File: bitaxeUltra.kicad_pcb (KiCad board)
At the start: 4 copper layers, 85 x 56 mm, 87 parts, among them J1 Barrel_Jack_Switch, J2 Conn_02x20_Odd_Even, J3 Conn_01x05, M1 Fan_4pin, Q1 CSD16321Q5, Q2 CSD16321Q5, Q3 BSS138, Q4 BSS138, Q5 BSS138, Q9 BSS138, U1 TPS40304DRC, U14 BM1366_mode1, U5 MCP1824T-1802E, U6 MCP1824T-0802E, U7 25MHz

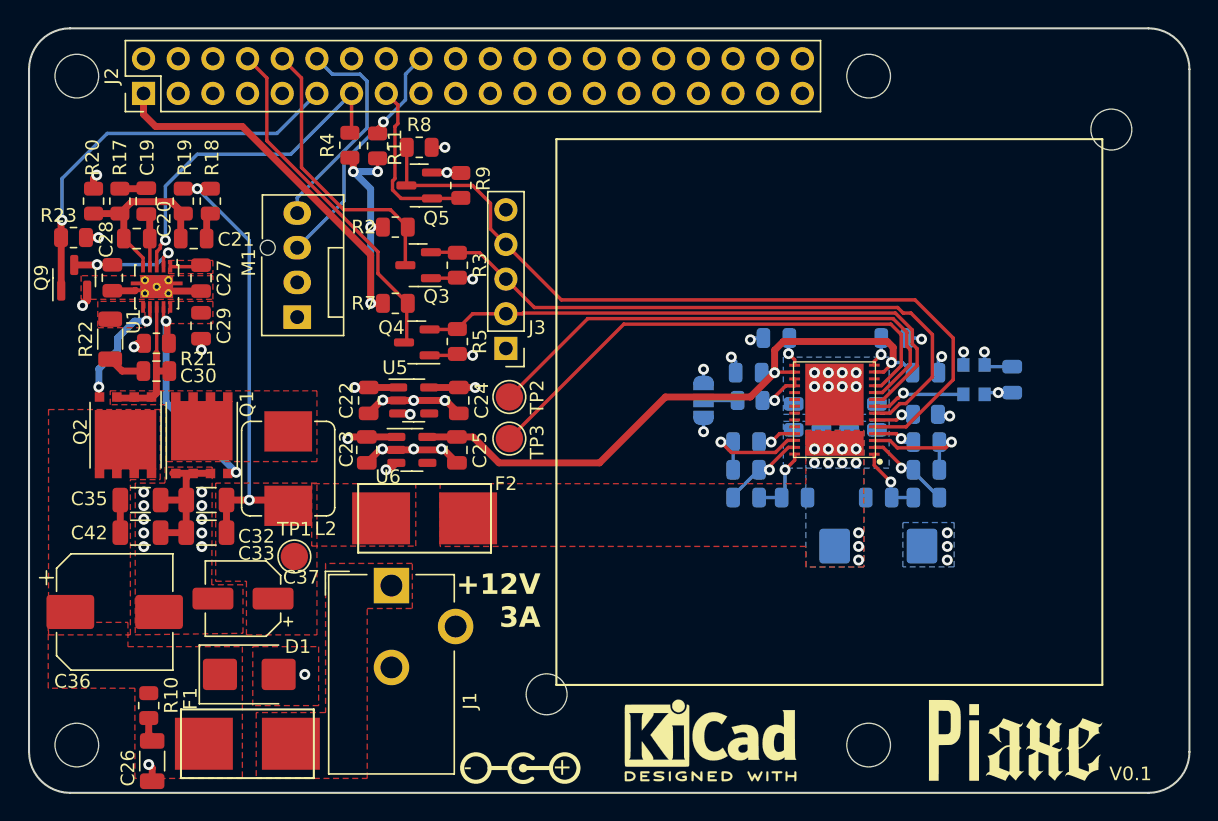
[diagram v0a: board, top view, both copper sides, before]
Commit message: added back the two 1uF
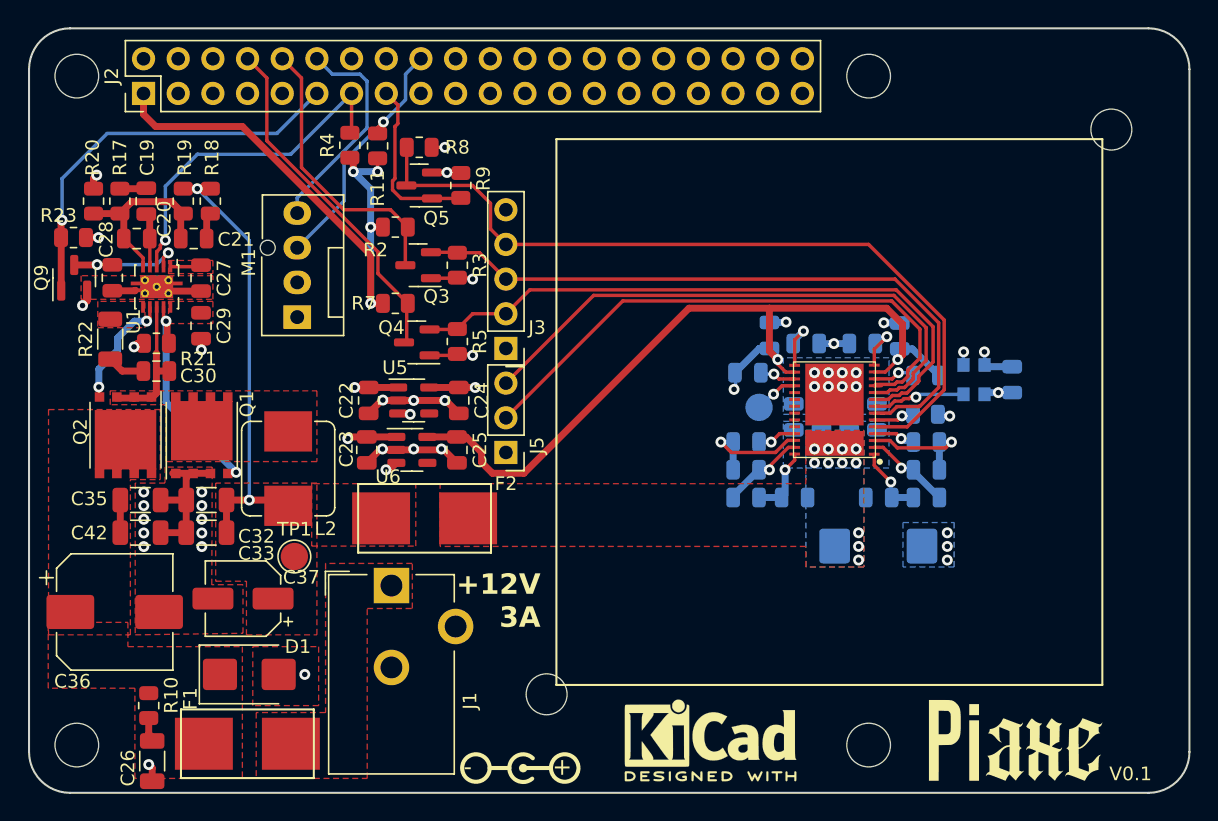
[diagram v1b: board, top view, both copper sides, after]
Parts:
- removed JP1: mode, Jumper:SolderJumper-3_P1.3mm_Open_RoundedPad1.0x1.5mm
- removed R1: 10k, Resistor_SMD:R_0805_2012Metric
- removed TP3: TEMP_n, TestPoint:TestPoint_Pad_D2.0mm
- added C31: 1µ, Capacitor_SMD:C_0805_2012Metric, B.Cu at (239.0, 81.2)
- added C34: 1µ, Capacitor_SMD:C_0805_2012Metric, B.Cu at (226.0, 81.0)
- added J5: temp, Connector_PinHeader_2.54mm:PinHeader_1x03_P2.54mm_Vertical, F.Cu at (208.3, 86.9)
- C32, C33: value 47µ -> 47µ/10V
- C35, C42: value 10µ -> 10µ/25V
- TP2: value TEMP_P -> TestPoint; moved to B.Cu
- moved TP2 18.3 mm to (226.8, 83.6), turned to 180 degrees
- moved C5 9.15 mm to (227.6, 78.3), turned to 90 degrees
- moved C16 8.60 mm to (234.4, 78.9)
- moved C4 3.28 mm to (237.1, 78.3), turned to 90 degrees
- moved C14 2.22 mm to (230.3, 78.9), turned to 0 degrees
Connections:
- C16 pad 1: +0V8 -> +1V8
- C5 pad 1: +1V8 -> +0V8
- TP2 pad 1: /BM1366/TEMP_P -> Net-(U14-MODE_0)
- U14 pad 12: unconnected-(U14-MODEO-Pad12) -> Net-(U14-MODEO)
- U14 pad 17: Net-(U14-MODE_0) -> Net-(U14-MODE_1)
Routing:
- net +0V8: track 46.8 -> 62.6 mm, vias 2 -> 3
- net /BM1366/TEMP_N: track 37.4 -> 41.8 mm
- net /BM1366/CI: track 43.3 -> 47.4 mm
- net /BM1366/TEMP_P: track 37.9 -> 41.8 mm
- net Net-(U14-MODEO): track 0.00 -> 3.11 mm, vias 0 -> 1
- net Net-(U14-MODE_1): track 0.00 -> 2.66 mm, vias 0 -> 1
- net Net-(JP1-C): track 2.49 -> 0.00 mm
- net +1V8: track 20.1 -> 22.2 mm, vias 9 -> 8
- net /BM1366/RO: track 47.7 -> 49.6 mm
- net GND: track 97.5 -> 96.4 mm, vias 42 -> 40

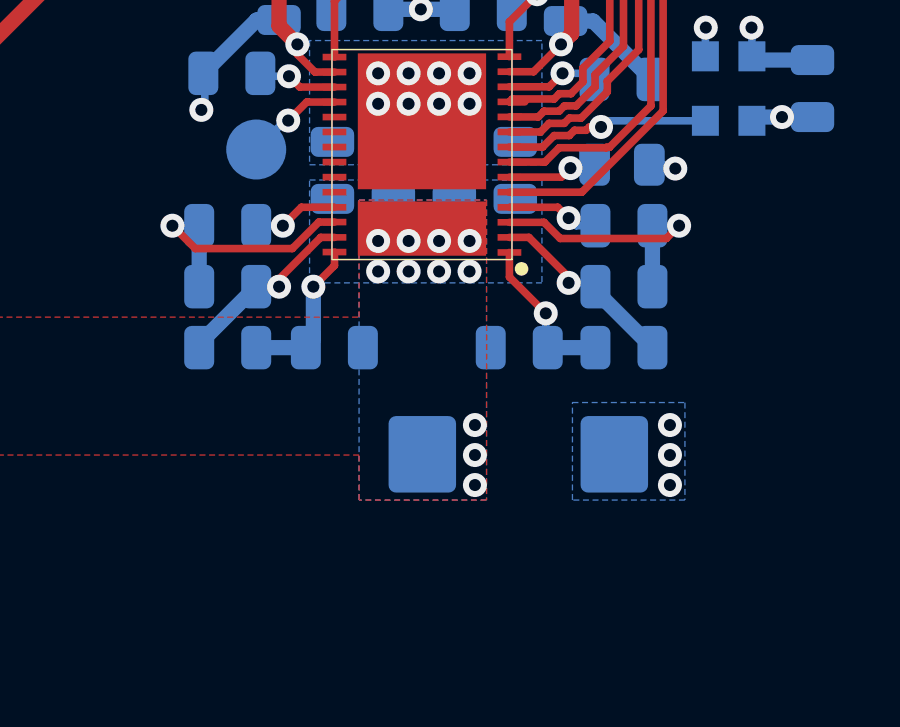
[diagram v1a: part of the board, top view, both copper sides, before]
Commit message: removed tantal and replaced with ceramic caps
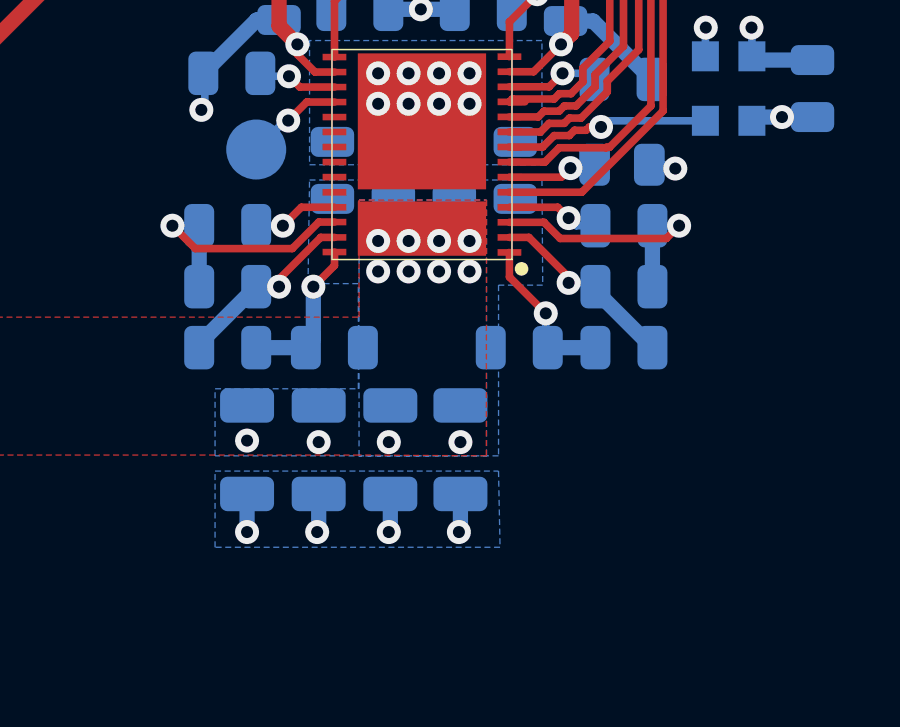
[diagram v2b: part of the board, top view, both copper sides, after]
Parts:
- removed C13: 330µ, Capacitor_Tantalum_SMD:CP_EIA-7343-31_Kemet-D_Pad2.25x2.55mm_HandSolder
- added C38: 10µ/25V, Capacitor_SMD:C_1206_3216Metric, B.Cu at (233.6, 93.6)
- added C39: 10µ/25V, Capacitor_SMD:C_1206_3216Metric, B.Cu at (231.3, 93.6)
- added C40: 47µ/10V, Capacitor_SMD:C_1206_3216Metric, B.Cu at (226.5, 93.6)
- added C41: 47µ/10V, Capacitor_SMD:C_1206_3216Metric, B.Cu at (228.9, 93.6)
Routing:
- net GND: track 96.4 -> 101.6 mm, vias 40 -> 41
- net +1V5: vias 11 -> 12

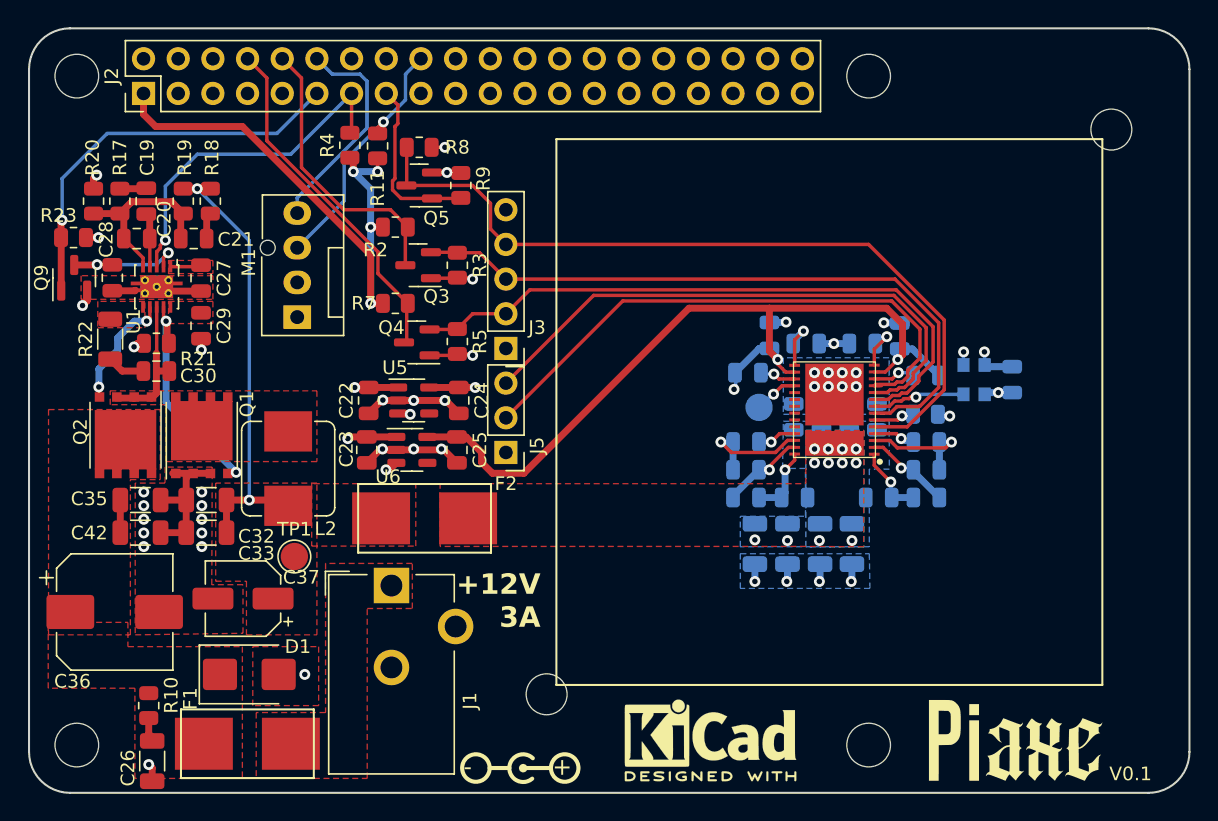
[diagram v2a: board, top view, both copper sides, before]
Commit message: revised heat-sinking. Supports heatsinks with 40x40 size with holes 35x35, 32x32 and 33x33
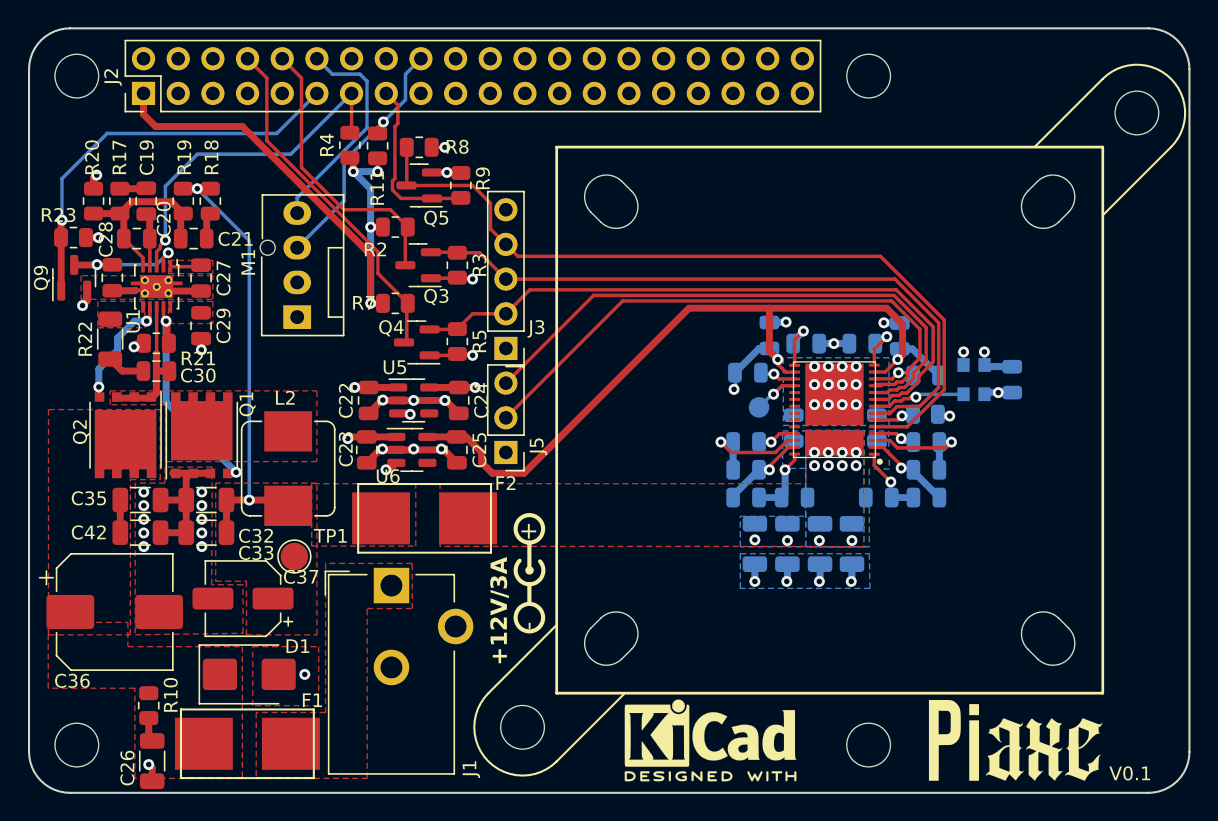
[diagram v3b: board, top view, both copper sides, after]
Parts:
- removed H5, H6: MountingHole, MountingHole:MountingHole_3.5mm
- added REF**: MountingHole_3.2mm_M3, MountingHole:MountingHole_3.2mm_M3, F.Cu at (254.5, 62.0)
- added REF**: MountingHole_3.2mm_M3, MountingHole:MountingHole_3.2mm_M3, F.Cu at (209.5, 107.0)
- TP2: footprint TestPoint:TestPoint_Pad_D2.0mm -> TestPoint:TestPoint_Pad_D1.5mm
- moved U3 14.5 mm to (210.0, 95.5), turned to 90 degrees
- moved C10 0.83 mm to (235.5, 85.1)
- moved C11 0.83 mm to (229.4, 85.1)
- moved C7 0.83 mm to (231.4, 85.1)
- moved C9 0.83 mm to (233.4, 85.1)
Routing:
- net GND: vias 41 -> 45
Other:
- outline, holes or cut-outs redrawn
- board text added: "+12V/3A"
- board text removed: "+12V 3A"

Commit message: added gerbers and bom
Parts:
- added C13: 100n, Capacitor_SMD:C_0805_2012Metric, B.Cu at (225.6, 78.3)
- added C43: 100n, Capacitor_SMD:C_0805_2012Metric, B.Cu at (239.1, 78.3)
- added C44: 100n, Capacitor_SMD:C_0805_2012Metric, B.Cu at (234.4, 76.9)
- added C45: 100n, Capacitor_SMD:C_0805_2012Metric, B.Cu at (230.3, 76.9)
- added JP1: SolderJumper_3_Open, Jumper:SolderJumper-3_P1.3mm_Open_RoundedPad1.0x1.5mm, F.Cu at (192.9, 80.5)
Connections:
- C27 pad 1: Net-(U1-VDD) -> +12V
- M1 pad 2: +5V -> Net-(JP1-C)
- U1 pad 1: Net-(U1-VDD) -> +12V
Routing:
- net +12V: track 2.39 -> 49.0 mm, vias 0 -> 4
- net GND: track 101.6 -> 109.4 mm
- net Net-(JP1-C): track 0.00 -> 7.57 mm
- net +5V: track 57.8 -> 63.3 mm
- net +1V8: track 22.2 -> 26.4 mm
- net +0V8: track 62.6 -> 66.6 mm
- net Net-(U1-VDD): track 2.29 -> 0.00 mm
- removed copper zone on F.Cu, net Net-(U1-VDD)

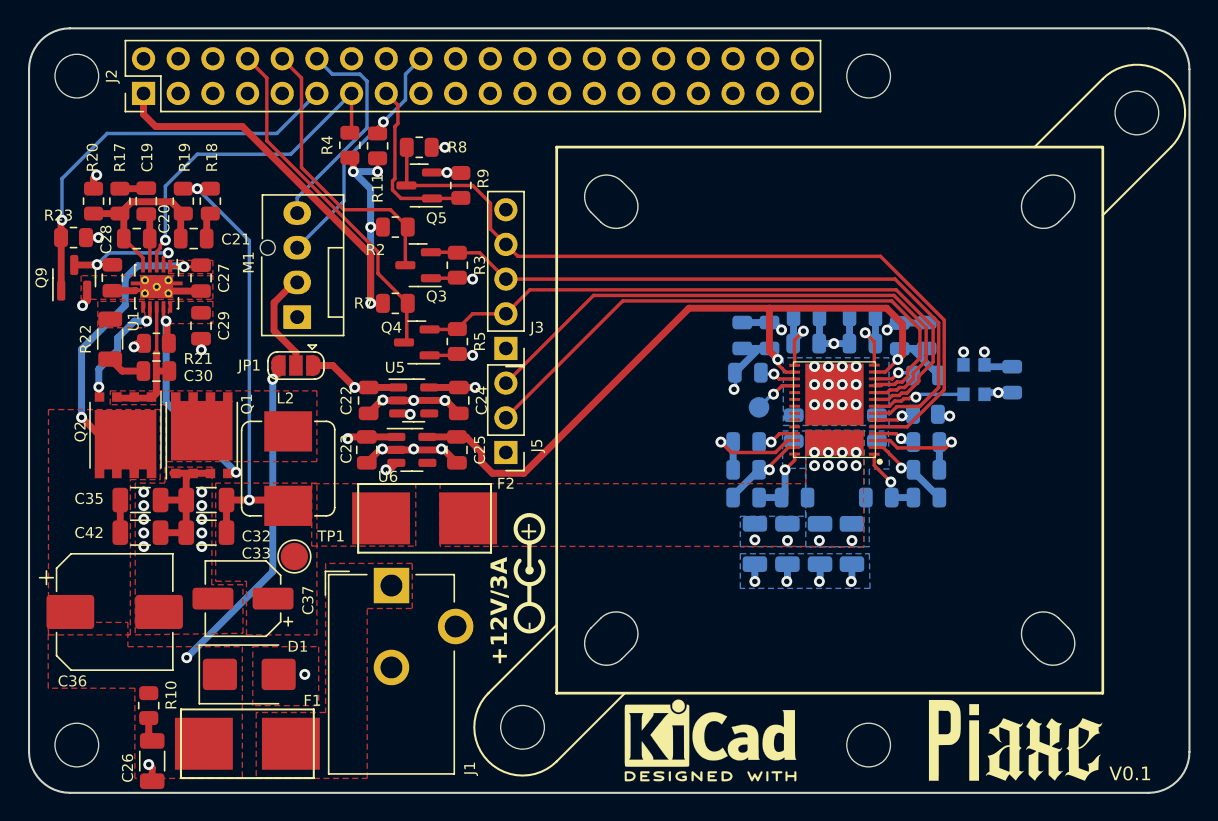
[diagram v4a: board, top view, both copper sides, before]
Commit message: fixed zone-edgecut clearance, added 2nd gnd layer and stitched them together for copper balance
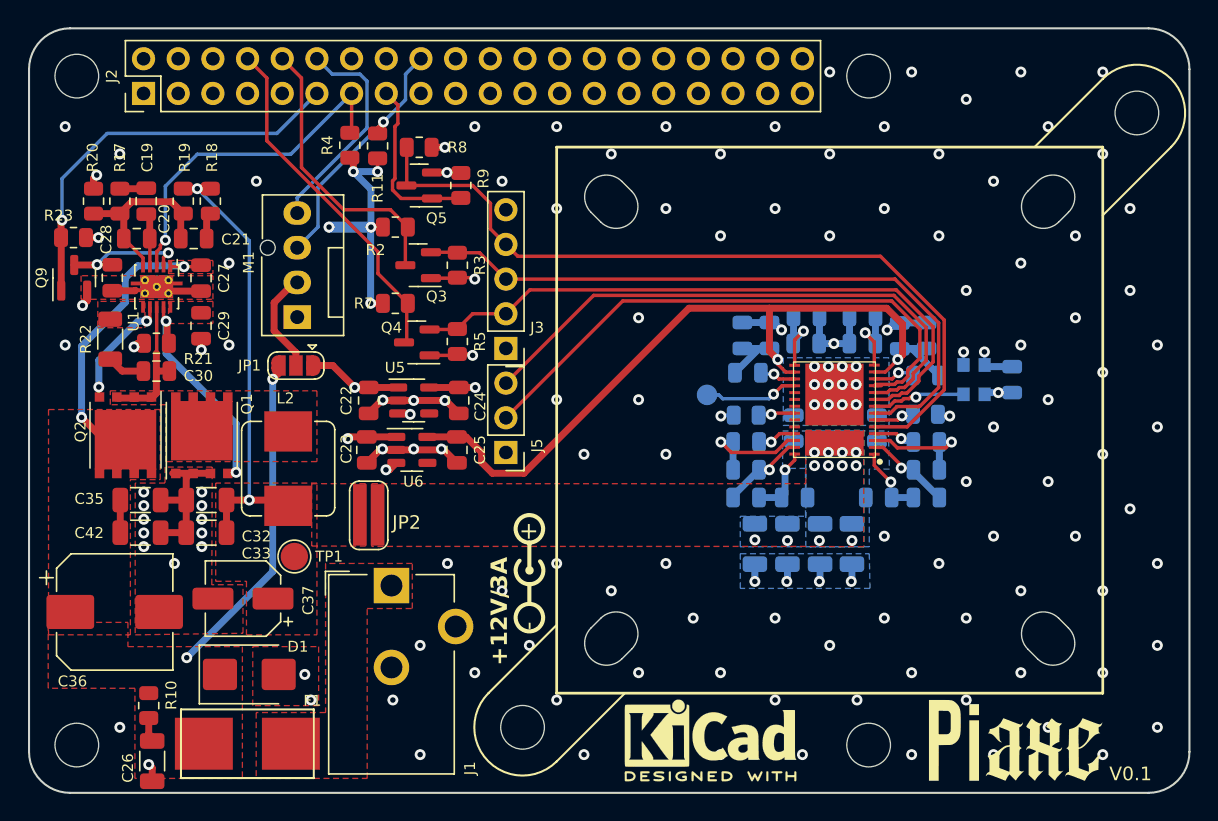
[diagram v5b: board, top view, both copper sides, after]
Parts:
- removed F2: 20A, myfootprints:fuseholder_littlefuse_blok
- added JP2: SolderJumper_2_Open, myfootprints:SolderJumper1.0x4.5, F.Cu at (198.4, 91.7)
- added R1: 10k, Resistor_SMD:R_0805_2012Metric, B.Cu at (225.9, 84.1)
- moved TP2 3.92 mm to (223.0, 82.7)
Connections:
- U14 pad 22: unconnected-(U14-RI-Pad22) -> Net-(U14-RI)
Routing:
- net +1V8: track 26.4 -> 97.5 mm, vias 8 -> 9
- net Net-(U14-MODE_0): track 3.26 -> 7.03 mm
- net +3V3: track 41.7 -> 38.4 mm, vias 4 -> 5
- net Net-(U14-RI): track 0.00 -> 2.70 mm, vias 0 -> 1
- net +0V8: track 66.6 -> 65.3 mm, vias 3 -> 2
- net +5V: track 63.3 -> 64.2 mm
- net GND: vias 45 -> 141
- added copper zone on In2.Cu, net GND
- removed copper zone on In2.Cu, net +1V8

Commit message: removed useless snubber
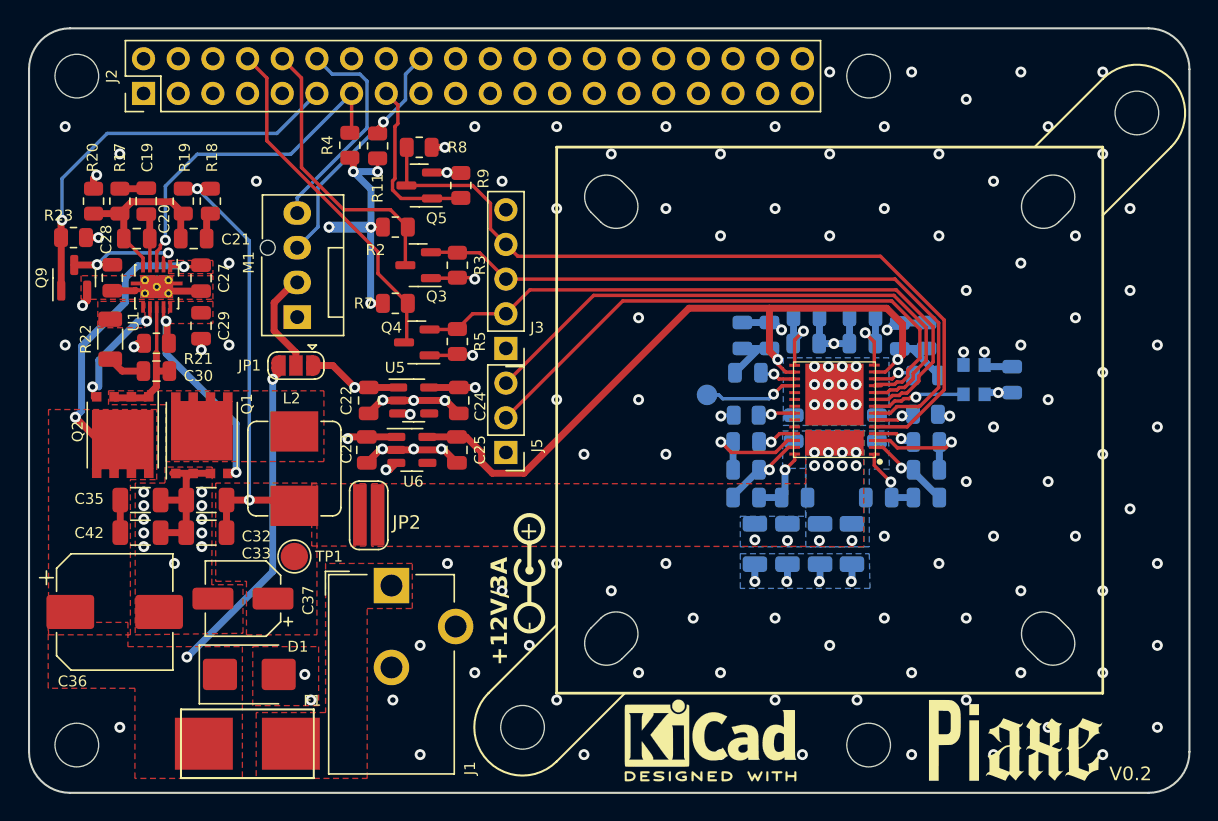
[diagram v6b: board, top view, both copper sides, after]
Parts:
- removed C26: 2.2/50V, Capacitor_SMD:C_1206_3216Metric
- removed R10: 2k, Resistor_SMD:R_0805_2012Metric
- moved L2 0.45 mm to (192.8, 88.1)
- moved Q2 0.20 mm to (180.2, 85.6)
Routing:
- net Net-(C26-Pad1): track 1.78 -> 0.00 mm
- net GND: track 109.4 -> 108.3 mm, vias 141 -> 140
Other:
- board text added: "V0.2"
- board text removed: "V0.1"
